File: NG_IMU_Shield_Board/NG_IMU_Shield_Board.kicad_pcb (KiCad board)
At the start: 2 copper layers, 87.6 x 45.7 mm, 20 parts, among them J1 Conn_01x04_Female, J2 Conn_01x02_Male, J3 Conn_01x10_Female, J4 Conn_01x03_Female, J6 Conn_01x11_Male, U1 SN75LBC175, U2 Level_Converter, U3 Teensy_v4.0

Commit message: Added BOM and Gerber files
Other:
- rule pad_to_mask_clearance: 0.2 -> 0
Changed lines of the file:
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@@
       (dielectric_constraints no)
     )
-    (pad_to_mask_clearance 0.2)
+    (pad_to_mask_clearance 0)
     (pcbplotparams
-      (layerselection 0x0000030_80000001)
+      (layerselection 0x00010ff_ffffffff)
       (disableapertmacros false)
       (usegerberextensions false)
@@
       (svguseinch false)
       (svgprecision 6)
-      (excludeedgelayer true)
+      (excludeedgelayer false)
       (plotframeref false)
       (viasonmask false)
@@
       (outputformat 1)
       (mirror false)
-      (drillshape 1)
+      (drillshape 0)
       (scaleselection 1)
       (outputdirectory "")
@@
     (fp_line (start 1 0.625) (end -1 0.625) (layer "F.Fab") (width 0.1))
     (fp_line (start -1 -0.625) (end 1 -0.625) (layer "F.Fab") (width 0.1))
-    (pad "1" smd roundrect (at -1 0 180) (size 1.2 1.4) (layers "F.Cu" "F.Paste" "F.Mask") (roundrect_rratio 0.208333)
+    (pad "1" smd roundrect (at -1 0 180) (size 1.2 1.4) (layers "F.Cu" "F.Paste" "F.Mask") (roundrect_rratio 0.2083333333)
       (net 47 "Net-(D2-Pad4)") (pintype "passive"))
-    (pad "2" smd roundrect (at 1 0 180) (size 1.2 1.4) (layers "F.Cu" "F.Paste" "F.Mask") (roundrect_rratio 0.208333)
+    (pad "2" smd roundrect (at 1 0 180) (size 1.2 1.4) (layers "F.Cu" "F.Paste" "F.Mask") (roundrect_rratio 0.2083333333)
       (net 38 "/RLED") (pintype "passive"))
     (model "${KICAD6_3DMODEL_DIR}/Resistor_SMD.3dshapes/R_0805_2012Metric.wrl"
@@
     (fp_line (start -1 0.625) (end -1 -0.625) (layer "F.Fab") (width 0.1))
     (fp_line (start 1 0.625) (end -1 0.625) (layer "F.Fab") (width 0.1))
-    (pad "1" smd roundrect (at -1 0 180) (size 1.2 1.4) (layers "F.Cu" "F.Paste" "F.Mask") (roundrect_rratio 0.208333)
+    (pad "1" smd roundrect (at -1 0 180) (size 1.2 1.4) (layers "F.Cu" "F.Paste" "F.Mask") (roundrect_rratio 0.2083333333)
       (net 45 "Net-(D2-Pad1)") (pintype "passive"))
-    (pad "2" smd roundrect (at 1 0 180) (size 1.2 1.4) (layers "F.Cu" "F.Paste" "F.Mask") (roundrect_rratio 0.208333)
+    (pad "2" smd roundrect (at 1 0 180) (size 1.2 1.4) (layers "F.Cu" "F.Paste" "F.Mask") (roundrect_rratio 0.2083333333)
       (net 40 "/GLED") (pintype "passive"))
     (model "${KICAD6_3DMODEL_DIR}/Resistor_SMD.3dshapes/R_0805_2012Metric.wrl"
@@
     (fp_line (start 1 -0.625) (end 1 0.625) (layer "F.Fab") (width 0.1))
     (fp_line (start -1 -0.625) (end 1 -0.625) (layer "F.Fab") (width 0.1))
-    (pad "1" smd roundrect (at -1 0 180) (size 1.2 1.4) (layers "F.Cu" "F.Paste" "F.Mask") (roundrect_rratio 0.208333)
+    (pad "1" smd roundrect (at -1 0 180) (size 1.2 1.4) (layers "F.Cu" "F.Paste" "F.Mask") (roundrect_rratio 0.2083333333)
       (net 46 "Net-(D2-Pad3)") (pintype "passive"))
-    (pad "2" smd roundrect (at 1 0 180) (size 1.2 1.4) (layers "F.Cu" "F.Paste" "F.Mask") (roundrect_rratio 0.208333)
+    (pad "2" smd roundrect (at 1 0 180) (size 1.2 1.4) (layers "F.Cu" "F.Paste" "F.Mask") (roundrect_rratio 0.2083333333)
       (net 39 "/BLED") (pintype "passive"))
     (model "${KICAD6_3DMODEL_DIR}/Resistor_SMD.3dshapes/R_0805_2012Metric.wrl"
@@
     (fp_line (start -1 0.625) (end 1 0.625) (layer "B.Fab") (width 0.1))
     (fp_line (start 1 -0.625) (end -1 -0.625) (layer "B.Fab") (width 0.1))
-    (pad "1" smd roundrect (at -1 0 270) (size 1.2 1.4) (layers "B.Cu" "B.Paste" "B.Mask") (roundrect_rratio 0.208333)
+    (pad "1" smd roundrect (at -1 0 270) (size 1.2 1.4) (layers "B.Cu" "B.Paste" "B.Mask") (roundrect_rratio 0.2083333333)
       (net 3 "Net-(D1-Pad2)") (pintype "passive"))
-    (pad "2" smd roundrect (at 1 0 270) (size 1.2 1.4) (layers "B.Cu" "B.Paste" "B.Mask") (roundrect_rratio 0.208333)
+    (pad "2" smd roundrect (at 1 0 270) (size 1.2 1.4) (layers "B.Cu" "B.Paste" "B.Mask") (roundrect_rratio 0.2083333333)
       (net 1 "/+5V") (pintype "passive"))
     (model "${KICAD6_3DMODEL_DIR}/Resistor_SMD.3dshapes/R_0805_2012Metric.wrl"
@@
     (fp_line (start 1.6 -0.8) (end -1.6 -0.8) (layer "B.Fab") (width 0.1))
     (fp_line (start -1.6 0.8) (end 1.6 0.8) (layer "B.Fab") (width 0.1))
-    (pad "1" smd roundrect (at -1.55 0 90) (size 1.3 1.75) (layers "B.Cu" "B.Paste" "B.Mask") (roundrect_rratio 0.192308)
+    (pad "1" smd roundrect (at -1.55 0 90) (size 1.3 1.75) (layers "B.Cu" "B.Paste" "B.Mask") (roundrect_rratio 0.1923076923)
       (net 20 "/Test+") (pintype "passive"))
-    (pad "2" smd roundrect (at 1.55 0 90) (size 1.3 1.75) (layers "B.Cu" "B.Paste" "B.Mask") (roundrect_rratio 0.192308)
+    (pad "2" smd roundrect (at 1.55 0 90) (size 1.3 1.75) (layers "B.Cu" "B.Paste" "B.Mask") (roundrect_rratio 0.1923076923)
       (net 21 "/Test-") (pintype "passive"))
     (model "${KICAD6_3DMODEL_DIR}/Resistor_SMD.3dshapes/R_1206_3216Metric.wrl"
@@
     (fp_line (start 1.6 0.8) (end 1.6 -0.8) (layer "B.Fab") (width 0.1))
     (fp_line (start -1.6 -0.8) (end -1.6 0.8) (layer "B.Fab") (width 0.1))
-    (pad "1" smd roundrect (at -1.55 0 90) (size 1.3 1.75) (layers "B.Cu" "B.Paste" "B.Mask") (roundrect_rratio 0.192308)
+    (pad "1" smd roundrect (at -1.55 0 90) (size 1.3 1.75) (layers "B.Cu" "B.Paste" "B.Mask") (roundrect_rratio 0.1923076923)
       (net 16 "/Ready-") (pintype "passive"))
-    (pad "2" smd roundrect (at 1.55 0 90) (size 1.3 1.75) (layers "B.Cu" "B.Paste" "B.Mask") (roundrect_rratio 0.192308)
+    (pad "2" smd roundrect (at 1.55 0 90) (size 1.3 1.75) (layers "B.Cu" "B.Paste" "B.Mask") (roundrect_rratio 0.1923076923)
       (net 17 "/Ready+") (pintype "passive"))
     (model "${KICAD6_3DMODEL_DIR}/Resistor_SMD.3dshapes/R_1206_3216Metric.wrl"

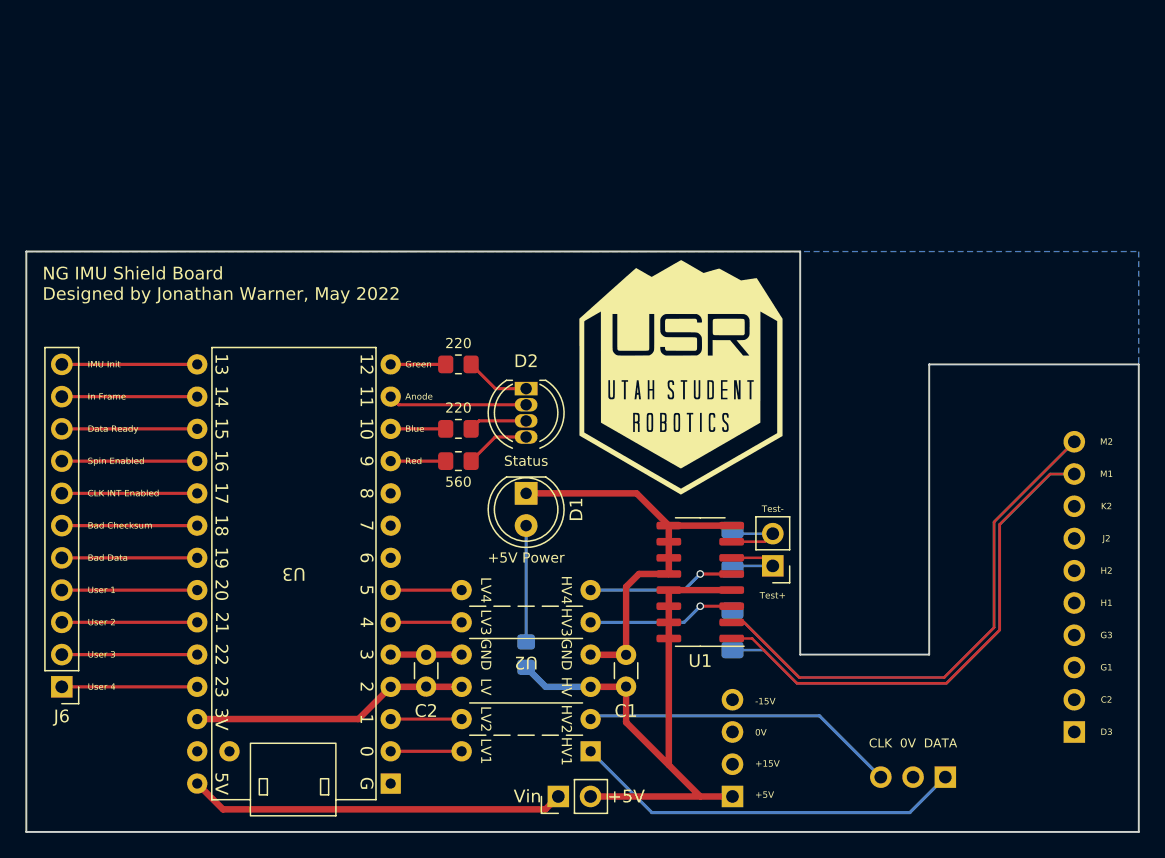
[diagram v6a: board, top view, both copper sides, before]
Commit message: Moved board to match original coordinates, added CTRL, and minor changes
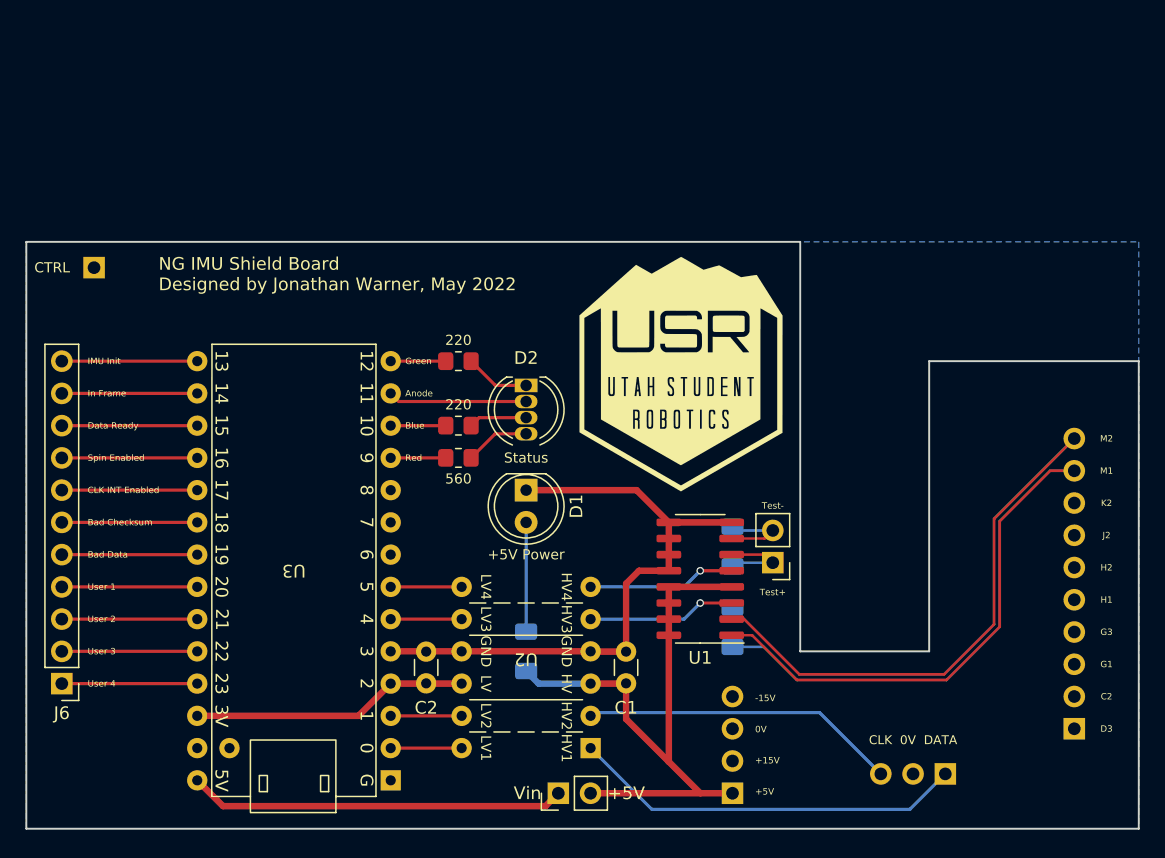
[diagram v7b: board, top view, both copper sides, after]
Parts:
- added J8: Conn_01x01_Female, Connector_PinSocket_2.54mm:PinSocket_1x01_P2.54mm_Vertical, B.Cu at (110.7, 59.9)
- R1: footprint Resistor_SMD:R_0805_2012Metric_Pad1.20x1.40mm_HandSolder -> Resistor_SMD:R_1206_3216Metric_Pad1.30x1.75mm_HandSolder
- moved C1 0.25 mm to (152.7, 92.7)
- moved C2 0.25 mm to (136.9, 92.7)
- moved D1 0.25 mm to (144.8, 77.5)
- moved D2 0.25 mm to (144.8, 69.2)
- moved G*** 0.25 mm to (157.0, 68.3)
- moved J6 0.25 mm to (108.2, 92.7)
- moved R1 0.25 mm to (144.8, 90.2)
- moved R4 0.25 mm to (139.4, 72.4)
- moved R5 0.25 mm to (161.0, 88.3)
- moved R6 0.25 mm to (161.0, 81.9)
- moved U1 0.25 mm to (158.5, 84.5)
- moved U2 0.25 mm to (144.8, 91.4)
- moved U3 0.25 mm to (134.1, 100.3)
- moved J1 0.25 mm to (161.0, 101.3)
- moved J2 0.25 mm to (164.2, 83.2)
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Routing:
- net /0V: track 38.6 -> 48.7 mm
- net Net-(D1-Pad2): track 9.16 -> 8.61 mm
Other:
- board size 87.6 x 45.7 mm -> 87.6 x 46.2 mm

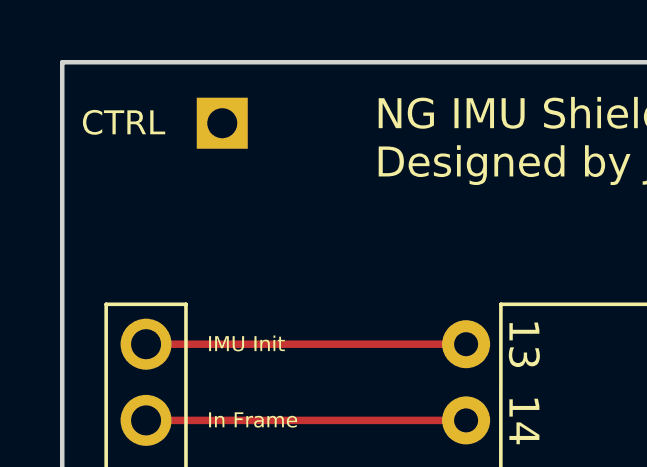
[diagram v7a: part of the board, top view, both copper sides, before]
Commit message: Added pin socket to allow disabling power with a jumper
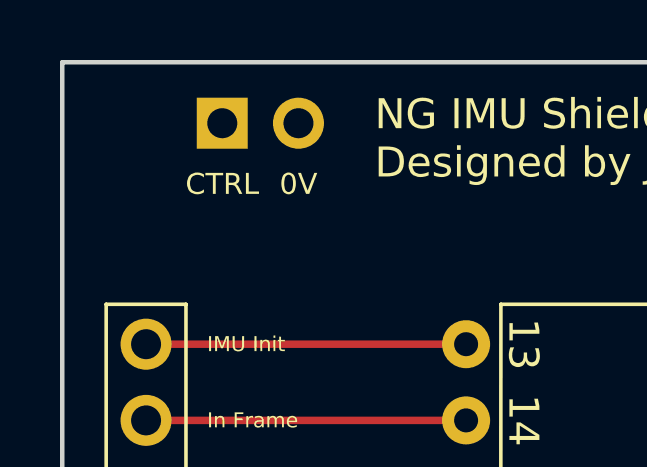
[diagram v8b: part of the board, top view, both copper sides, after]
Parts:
- J8: value Conn_01x01_Female -> Conn_01x02_Female; footprint Connector_PinSocket_2.54mm:PinSocket_1x01_P2.54mm_Vertical -> Connector_PinSocket_2.54mm:PinSocket_1x02_P2.54mm_Vertical
- turned J8 to -90 degrees
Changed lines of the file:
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@@
     )
   )
-  (footprint "Connector_PinSocket_2.54mm:PinSocket_1x01_P2.54mm_Vertical" (layer "B.Cu")
-    (at 110.744 59.944)
-    (descr "Through hole straight socket strip, 1x01, 2.54mm pitch, single row (from Kicad 4.0.7), script generated")
-    (tags "Through hole socket strip THT 1x01 2.54mm single row")
+  (footprint "Connector_PinSocket_2.54mm:PinSocket_1x02_P2.54mm_Vertical" (layer "B.Cu")
+    (at 110.744 59.944 -90)
+    (descr "Through hole straight socket strip, 1x02, 2.54mm pitch, single row (from Kicad 4.0.7), script generated")
+    (tags "Through hole socket strip THT 1x02 2.54mm single row")
     (property "Sheetfile" "NG_IMU_Shield_Board.kicad_sch")
     (property "Sheetname" "")
     (attr through_hole)
-    (fp_text reference "J8" (at 2.54 0 270) (layer "B.SilkS")
+    (fp_text reference "J8" (at 0 2.77 90) (layer "B.SilkS")
       (effects (font (size 1 1) (thickness 0.15)) (justify mirror))
     )
-    (fp_text value "Conn_01x01_Female" (at 0 -2.77 180) (layer "B.Fab")
+    (fp_text value "Conn_01x02_Female" (at 0 -5.31 90) (layer "B.Fab")
       (effects (font (size 1 1) (thickness 0.15)) (justify mirror))
     )
-    (fp_text user "CTRL" (at -3.302 0 unlocked) (layer "F.SilkS")
-      (effects (font (size 0.8 0.8) (thickness 0.08)))
+    (fp_text user "CTRL" (at 2.032 0 unlocked) (layer "F.SilkS")
+      (effects (font (size 0.7 0.7) (thickness 0.07)))
     )
-    (fp_text user "${REFERENCE}" (at 0 0 180) (layer "B.Fab")
+    (fp_text user "0V" (at 2.032 -2.54 unlocked) (layer "F.SilkS")
+      (effects (font (size 0.7 0.7) (thickness 0.07)))
+    )
+    (fp_text user "${REFERENCE}" (at 0 -1.27) (layer "B.Fab")
       (effects (font (size 1 1) (thickness 0.15)) (justify mirror))
     )
     (fp_line (start 1.33 1.33) (end 1.33 0) (layer "B.SilkS") (width 0.12))
-    (fp_line (start 1.33 -1.21) (end 1.33 -1.33) (layer "B.SilkS") (width 0.12))
-    (fp_line (start -1.33 -1.21) (end -1.33 -1.33) (layer "B.SilkS") (width 0.12))
     (fp_line (start 0 1.33) (end 1.33 1.33) (layer "B.SilkS") (width 0.12))
-    (fp_line (start -1.33 -1.33) (end 1.33 -1.33) (layer "B.SilkS") (width 0.12))
-    (fp_line (start 1.75 -1.75) (end -1.8 -1.75) (layer "B.CrtYd") (width 0.05))
+    (fp_line (start 1.33 -1.27) (end 1.33 -3.87) (layer "B.SilkS") (width 0.12))
+    (fp_line (start -1.33 -3.87) (end 1.33 -3.87) (layer "B.SilkS") (width 0.12))
+    (fp_line (start -1.33 -1.27) (end 1.33 -1.27) (layer "B.SilkS") (width 0.12))
+    (fp_line (start -1.33 -1.27) (end -1.33 -3.87) (layer "B.SilkS") (width 0.12))
+    (fp_line (start -1.8 -4.3) (end -1.8 1.8) (layer "B.CrtYd") (width 0.05))
+    (fp_line (start 1.75 1.8) (end 1.75 -4.3) (layer "B.CrtYd") (width 0.05))
     (fp_line (start -1.8 1.8) (end 1.75 1.8) (layer "B.CrtYd") (width 0.05))
-    (fp_line (start 1.75 1.8) (end 1.75 -1.75) (layer "B.CrtYd") (width 0.05))
-    (fp_line (start -1.8 -1.75) (end -1.8 1.8) (layer "B.CrtYd") (width 0.05))
-    (fp_line (start 1.27 -1.27) (end -1.27 -1.27) (layer "B.Fab") (width 0.1))
+    (fp_line (start 1.75 -4.3) (end -1.8 -4.3) (layer "B.CrtYd") (width 0.05))
     (fp_line (start 0.635 1.27) (end 1.27 0.635) (layer "B.Fab") (width 0.1))
-    (fp_line (start -1.27 -1.27) (end -1.27 1.27) (layer "B.Fab") (width 0.1))
-    (fp_line (start 1.27 0.635) (end 1.27 -1.27) (layer "B.Fab") (width 0.1))
     (fp_line (start -1.27 1.27) (end 0.635 1.27) (layer "B.Fab") (width 0.1))
-    (pad "1" thru_hole rect (at 0 0) (size 1.7 1.7) (drill 1) (layers *.Cu *.Mask)
+    (fp_line (start 1.27 -3.81) (end -1.27 -3.81) (layer "B.Fab") (width 0.1))
+    (fp_line (start 1.27 0.635) (end 1.27 -3.81) (layer "B.Fab") (width 0.1))
+    (fp_line (start -1.27 -3.81) (end -1.27 1.27) (layer "B.Fab") (width 0.1))
+    (pad "1" thru_hole rect (at 0 0 270) (size 1.7 1.7) (drill 1) (layers *.Cu *.Mask)
       (net 50 "/CTRL") (pinfunction "Pin_1") (pintype "passive"))
-    (model "${KICAD6_3DMODEL_DIR}/Connector_PinSocket_2.54mm.3dshapes/PinSocket_1x01_P2.54mm_Vertical.wrl"
+    (pad "2" thru_hole oval (at 0 -2.54 270) (size 1.7 1.7) (drill 1) (layers *.Cu *.Mask)
+      (net 2 "/0V") (pinfunction "Pin_2") (pintype "passive"))
+    (model "${KICAD6_3DMODEL_DIR}/Connector_PinSocket_2.54mm.3dshapes/PinSocket_1x02_P2.54mm_Vertical.wrl"
       (offset (xyz 0 0 0))
       (scale (xyz 1 1 1))
